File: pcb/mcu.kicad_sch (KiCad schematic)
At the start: 19 parts, among them J4 AVR-UPDI-6, U4 ATtiny1616-MNR

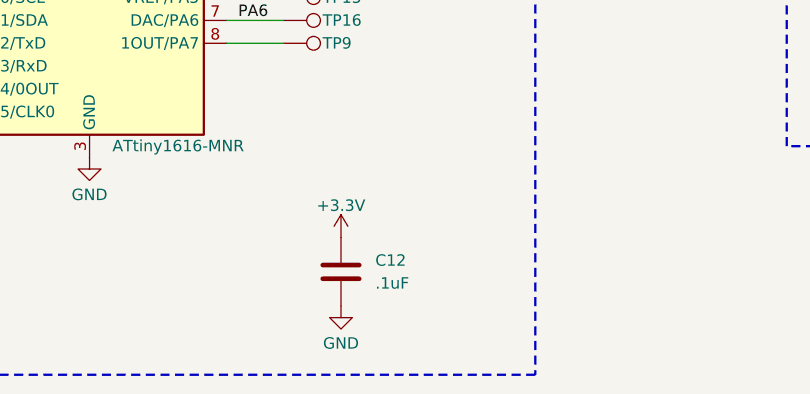
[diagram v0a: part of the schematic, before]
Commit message: Fixed LCSC part numbers and attributes
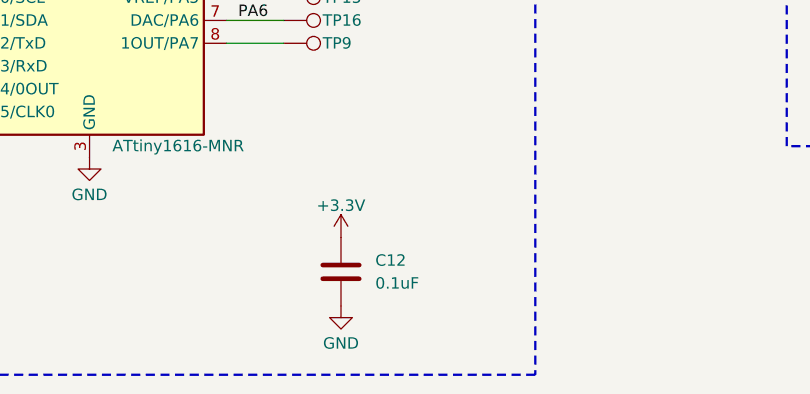
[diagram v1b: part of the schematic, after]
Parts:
- C12: value .1uF -> 0.1uF; LCSC C15849 -> C66501; MPN CL10A105KB8NNNC -> CL10B104KO8NNNC; Tolerance (none) -> 10%
- R13, R14: Tolerance (none) -> 5%
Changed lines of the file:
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@@
 			)
 		)
-		(property "Value" ".1uF"
+		(property "Value" "0.1uF"
 			(at 132.08 88.8999 0)
 			(effects
@@
 			)
 		)
-		(property "MPN" "CL10A105KB8NNNC"
+		(property "MPN" "CL10B104KO8NNNC"
 			(at 128.27 87.63 0)
 			(effects
@@
 			)
 		)
-		(property "LCSC" "C15849"
+		(property "LCSC" "C66501"
 			(at 128.27 87.63 0)
 			(effects
@@
 		)
 		(property "Mouser" "187-CL10A105KB8NNNC"
+			(at 128.27 87.63 0)
+			(effects
+				(font
+					(size 1.27 1.27)
+				)
+				(hide yes)
+			)
+		)
+		(property "Tolerance" "10%"
 			(at 128.27 87.63 0)
 			(effects
@@
 			)
 		)
+		(property "Tolerance" "5%"
+			(at 64.77 52.07 0)
+			(effects
+				(font
+					(size 1.27 1.27)
+				)
+				(hide yes)
+			)
+		)
 		(pin "2"
 		)
@@
 			(at 49.53 52.07 0)
 			(effects
+				(font
+					(size 1.27 1.27)
+				)
+				(hide yes)
+			)
+		)
+		(property "Tolerance" "5%"
+			(at 49.53 52.07 0)
+			(effects

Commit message: Adjusted BOM settings
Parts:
- C12: Digikey 1276-1860-2-ND -> 1276-1005-2-ND; Mouser 187-CL10A105KB8NNNC -> 187-CL10B104KO8NNNC; Vr (none) -> 16V
- TP10, TP11, TP12, TP13, TP14, TP15, TP16, TP18, TP7, TP8, TP9: now left out of the parts list
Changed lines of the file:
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@@
 		(unit 1)
 		(exclude_from_sim no)
-		(in_bom yes)
+		(in_bom no)
 		(on_board yes)
 		(dnp no)
@@
 		(unit 1)
 		(exclude_from_sim no)
-		(in_bom yes)
+		(in_bom no)
 		(on_board yes)
 		(dnp no)
@@
 		(unit 1)
 		(exclude_from_sim no)
-		(in_bom yes)
+		(in_bom no)
 		(on_board yes)
 		(dnp no)
@@
 		(unit 1)
 		(exclude_from_sim no)
-		(in_bom yes)
+		(in_bom no)
 		(on_board yes)
 		(dnp no)
@@
 			)
 		)
-		(property "Digikey" "1276-1860-2-ND"
+		(property "Digikey" "1276-1005-2-ND"
 			(at 128.27 87.63 0)
 			(effects
@@
 			)
 		)
-		(property "Mouser" "187-CL10A105KB8NNNC"
+		(property "Mouser" "187-CL10B104KO8NNNC"
 			(at 128.27 87.63 0)
 			(effects
@@
 		)
 		(property "Tolerance" "10%"
+			(at 128.27 87.63 0)
+			(effects
+				(font
+					(size 1.27 1.27)
+				)
+				(hide yes)
+			)
+		)
+		(property "Vr" "16V"
 			(at 128.27 87.63 0)
 			(effects
@@
 		(unit 1)
 		(exclude_from_sim no)
-		(in_bom yes)
+		(in_bom no)
 		(on_board yes)
 		(dnp no)
@@
 		(property "Description" "Test Point D1.0mm"
 			(at 195.58 47.244 0)
+			(effects
+				(font
+					(size 1.27 1.27)
+				)
+				(hide yes)
+			)
+		)
+		(property "LCSC" ""
+			(at 195.58 38.1 0)
+			(effects
+				(font
+					(size 1.27 1.27)
+				)
+				(hide yes)
+			)
+		)
+		(property "Digikey" ""
+			(at 195.58 38.1 0)
+			(effects
+				(font
+					(size 1.27 1.27)
+				)
+				(hide yes)
+			)
+		)
+		(property "Mouser" ""
+			(at 195.58 38.1 0)
 			(effects
 				(font
@@
 		(unit 1)
 		(exclude_from_sim no)
-		(in_bom yes)
+		(in_bom no)
 		(on_board yes)
 		(dnp no)
@@
 		(unit 1)
 		(exclude_from_sim no)
-		(in_bom yes)
+		(in_bom no)
 		(on_board yes)
 		(dnp no)
@@
 		(unit 1)
 		(exclude_from_sim no)
-		(in_bom yes)
+		(in_bom no)
 		(on_board yes)
 		(dnp no)
@@
 		(unit 1)
 		(exclude_from_sim no)
-		(in_bom yes)
+		(in_bom no)
 		(on_board yes)
 		(dnp no)
@@
 		(unit 1)
 		(exclude_from_sim no)
-		(in_bom yes)
+		(in_bom no)
 		(on_board yes)
 		(dnp no)
@@
 		(unit 1)
 		(exclude_from_sim no)
-		(in_bom yes)
-		(on_board yes)
-		(dnp no)
+		(in_bom no)
+		(on_board yes)
+		(dnp no)

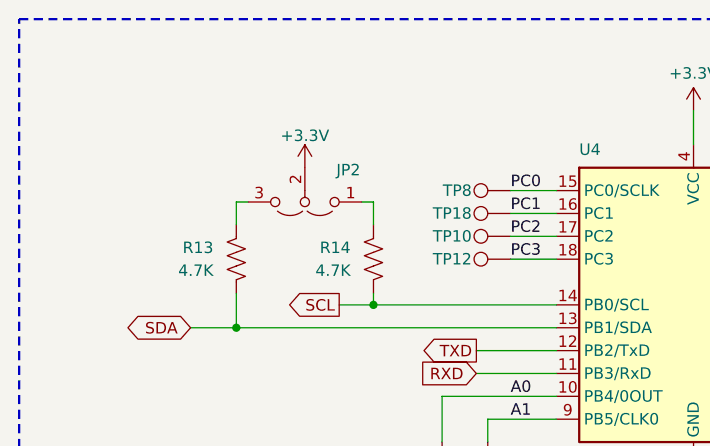
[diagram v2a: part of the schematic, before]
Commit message: Tightened to 50mm wide
SO MUCH fiddling!
Changed I2C to single jumpers
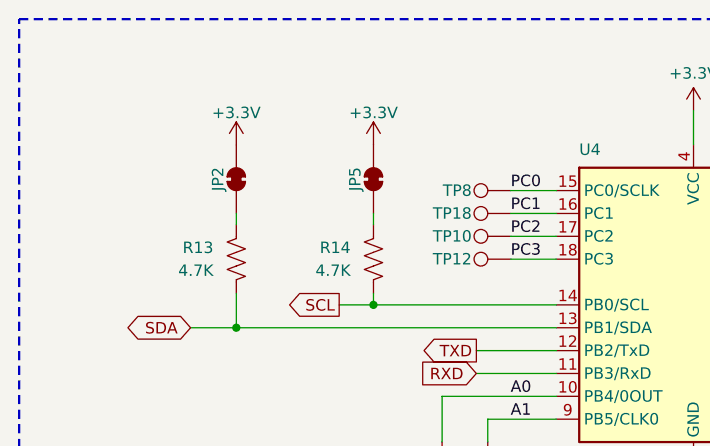
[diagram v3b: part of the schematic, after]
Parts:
- removed JP2: ~, CRGM Connector:SolderJumper-3_P1.3mm_Open_RoundedPad1.0x1.5mm, symbol Jumper:Jumper_3_Open
- added JP2, JP5: ~, CRGM Connector:SolderJumper-2_P1.3mm_Bridged_RoundedPad1.0x1.5mm, symbol Jumper:SolderJumper_2_Bridged
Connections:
- net +3.3V: now also JP2.2 (B), JP5.2 (B)
- net at R14.2: now also JP5.1 (A)
- net at R13.2: now also JP2.1 (A)
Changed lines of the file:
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@@
 	(wire
 		(pts
-			(xy 64.77 45.72) (xy 64.77 48.26)
+			(xy 64.77 46.99) (xy 64.77 48.26)
 		)
 		(stroke
@@
 	(wire
 		(pts
-			(xy 63.5 45.72) (xy 64.77 45.72)
-		)
-		(stroke
-			(width 0)
-			(type default)
-		)
-	)
-	(wire
-		(pts
 			(xy 217.17 46.99) (xy 220.98 46.99)
 		)
@@
 	(wire
 		(pts
-			(xy 50.8 45.72) (xy 49.53 45.72)
-		)
-		(stroke
-			(width 0)
-			(type default)
-		)
-	)
-	(wire
-		(pts
 			(xy 49.53 59.69) (xy 85.09 59.69)
 		)
@@
 	(wire
 		(pts
-			(xy 49.53 45.72) (xy 49.53 48.26)
+			(xy 49.53 46.99) (xy 49.53 48.26)
 		)
 		(stroke
@@
 				(path "/a8149920-3b7f-4d7d-8e96-7a0b38870225/573c51ea-89ab-4745-b6d8-c69e780cd603"
 					(reference "TP10")
+					(unit 1)
+				)
+			)
+		)
+	)
+	(symbol
+		(lib_id "Jumper:SolderJumper_2_Bridged")
+		(at 64.77 43.18 90)
+		(unit 1)
+		(exclude_from_sim no)
+		(in_bom no)
+		(on_board yes)
+		(dnp no)
+		(property "Reference" "JP5"
+			(at 62.738 43.18 0)
+			(effects
+				(font
+					(size 1.27 1.27)
+				)
+			)
+		)
+		(property "Value" "~"
+			(at 67.31 43.18 0)
+			(effects
+				(font
+					(size 1.27 1.27)
+				)
+				(hide yes)
+			)
+		)
+		(property "Footprint" "CRGM Connector:SolderJumper-2_P1.3mm_Bridged_RoundedPad1.0x1.5mm"
+			(at 64.77 43.18 0)
+			(effects
+				(font
+					(size 1.27 1.27)
+				)
+				(hide yes)
+			)
+		)
+		(property "Datasheet" "~"
+			(at 64.77 43.18 0)
+			(effects
+				(font
+					(size 1.27 1.27)
+				)
+				(hide yes)
+			)
+		)
+		(property "Description" "Solder Jumper, 2-pole, closed/bridged"
+			(at 64.77 43.18 0)
+			(effects
+				(font
+					(size 1.27 1.27)
+				)
+				(hide yes)
+			)
+		)
+		(property "LCSC" ""
+			(at 64.77 43.18 0)
+			(effects
+				(font
+					(size 1.27 1.27)
+				)
+				(hide yes)
+			)
+		)
+		(property "Digikey" ""
+			(at 64.77 43.18 0)
+			(effects
+				(font
+					(size 1.27 1.27)
+				)
+				(hide yes)
+			)
+		)
+		(property "Mouser" ""
+			(at 64.77 43.18 0)
+			(effects
+				(font
+					(size 1.27 1.27)
+				)
+				(hide yes)
+			)
+		)
+		(pin "2"
+		)
+		(pin "1"
+		)
+		(instances
+			(project "current-module"
+				(path "/a8149920-3b7f-4d7d-8e96-7a0b38870225/573c51ea-89ab-4745-b6d8-c69e780cd603"
+					(reference "JP5")
 					(unit 1)
 				)
@@
 	)
 	(symbol
-		(lib_id "Jumper:Jumper_3_Open")
-		(at 57.15 45.72 180)
-		(unit 1)
-		(exclude_from_sim no)
-		(in_bom no)
-		(on_board yes)
-		(dnp no)
-		(property "Reference" "JP2"
-			(at 61.976 42.164 0)
-			(effects
-				(font
-					(size 1.27 1.27)
-				)
-			)
-		)
-		(property "Value" "~"
-			(at 48.006 42.418 0)
-			(effects
-				(font
-					(size 1.27 1.27)
-				)
-			)
-		)
-		(property "Footprint" "CRGM Connector:SolderJumper-3_P1.3mm_Open_RoundedPad1.0x1.5mm"
-			(at 57.15 45.72 0)
-			(effects
-				(font
-					(size 1.27 1.27)
-				)
-				(hide yes)
-			)
-		)
-		(property "Datasheet" "~"
-			(at 57.15 45.72 0)
-			(effects
-				(font
-					(size 1.27 1.27)
-				)
-				(hide yes)
-			)
-		)
-		(property "Description" "Jumper, 3-pole, both open"
-			(at 57.15 45.72 0)
-			(effects
-				(font
-					(size 1.27 1.27)
-				)
-				(hide yes)
-			)
-		)
-		(property "MPN" ""
-			(at 57.15 45.72 0)
-			(effects
-				(font
-					(size 1.27 1.27)
-				)
-				(hide yes)
-			)
-		)
-		(property "LCSC" ""
-			(at 57.15 45.72 0)
-			(effects
-				(font
-					(size 1.27 1.27)
-				)
-				(hide yes)
-			)
-		)
-		(property "Digikey" ""
-			(at 57.15 45.72 0)
-			(effects
-				(font
-					(size 1.27 1.27)
-				)
-				(hide yes)
-			)
-		)
-		(property "Mouser" ""
-			(at 57.15 45.72 0)
-			(effects
-				(font
-					(size 1.27 1.27)
-				)
-				(hide yes)
-			)
-		)
-		(pin "3"
-		)
-		(pin "1"
-		)
-		(pin "2"
-		)
-		(instances
-			(project "relay-module"
-				(path "/445c1fff-2e1a-48b1-a91f-a137832edebf/3b602092-7627-4b1e-9a45-58db61fac69b"
-					(reference "JP1")
-					(unit 1)
-				)
-			)
-			(project ""
-				(path "/a8149920-3b7f-4d7d-8e96-7a0b38870225/573c51ea-89ab-4745-b6d8-c69e780cd603"
-					(reference "JP2")
-					(unit 1)
-				)
-			)
-		)
-	)
-	(symbol
 		(lib_id "power:+3.3V")
-		(at 57.15 41.91 0)
+		(at 49.53 39.37 0)
 		(mirror y)
 		(unit 1)
@@
 		(dnp no)
 		(property "Reference" "#PWR0107"
-			(at 57.15 45.72 0)
+			(at 49.53 43.18 0)
 			(effects
 				(font
@@
 		)
 		(property "Value" "+3.3V"
-			(at 57.15 38.354 0)
+			(at 49.53 35.814 0)
 			(effects
 				(font
@@
 		)
 		(property "Footprint" ""
-			(at 57.15 41.91 0)
+			(at 49.53 39.37 0)
 			(effects
 				(font
@@
 		)
 		(property "Datasheet" ""
-			(at 57.15 41.91 0)
+			(at 49.53 39.37 0)
 			(effects
 				(font
@@
 		)
 		(property "Description" "Power symbol creates a global label with name \"+3.3V\""
-			(at 57.15 41.91 0)
+			(at 49.53 39.37 0)
 			(effects
 				(font
@@
 				(path "/a8149920-3b7f-4d7d-8e96-7a0b38870225/573c51ea-89ab-4745-b6d8-c69e780cd603"
 					(reference "#PWR0107")
+					(unit 1)
+				)
+			)
+		)
+	)
+	(symbol
+		(lib_id "power:+3.3V")
+		(at 64.77 39.37 0)
+		(mirror y)
+		(unit 1)
+		(exclude_from_sim no)
+		(in_bom yes)
+		(on_board yes)
+		(dnp no)
+		(property "Reference" "#PWR03"
+			(at 64.77 43.18 0)
+			(effects
+				(font
+					(size 1.27 1.27)
+				)
+				(hide yes)
+			)
+		)
+		(property "Value" "+3.3V"
+			(at 64.77 35.814 0)
+			(effects
+				(font
+					(size 1.27 1.27)
+				)
+			)
+		)
+		(property "Footprint" ""
+			(at 64.77 39.37 0)
+			(effects
+				(font
+					(size 1.27 1.27)
+				)
+				(hide yes)
+			)
+		)
+		(property "Datasheet" ""
+			(at 64.77 39.37 0)
+			(effects
+				(font
+					(size 1.27 1.27)
+				)
+				(hide yes)
+			)
+		)
+		(property "Description" "Power symbol creates a global label with name \"+3.3V\""
+			(at 64.77 39.37 0)
+			(effects
+				(font
+					(size 1.27 1.27)
+				)
+				(hide yes)
+			)
+		)
+		(pin "1"
+		)
+		(instances
+			(project "current-module"
+				(path "/a8149920-3b7f-4d7d-8e96-7a0b38870225/573c51ea-89ab-4745-b6d8-c69e780cd603"
+					(reference "#PWR03")
 					(unit 1)
 				)
@@
 					(unit 1)
 				)
+			)
+		)
+	)
+	(symbol
+		(lib_id "Jumper:SolderJumper_2_Bridged")
+		(at 49.53 43.18 90)
+		(unit 1)
+		(exclude_from_sim no)
+		(in_bom no)
+		(on_board yes)
+		(dnp no)
+		(property "Reference" "JP2"
+			(at 47.498 43.18 0)
+			(effects
+				(font
+					(size 1.27 1.27)
+				)
+			)
+		)
+		(property "Value" "~"
+			(at 52.07 43.18 0)
+			(effects
+				(font
+					(size 1.27 1.27)
+				)
+				(hide yes)
+			)
+		)
+		(property "Footprint" "CRGM Connector:SolderJumper-2_P1.3mm_Bridged_RoundedPad1.0x1.5mm"
+			(at 49.53 43.18 0)
+			(effects
+				(font
+					(size 1.27 1.27)
+				)
+				(hide yes)
+			)
+		)
+		(property "Datasheet" "~"
+			(at 49.53 43.18 0)
+			(effects
+				(font
+					(size 1.27 1.27)
+				)
+				(hide yes)
+			)
+		)
+		(property "Description" "Solder Jumper, 2-pole, closed/bridged"
+			(at 49.53 43.18 0)
+			(effects
+				(font
+					(size 1.27 1.27)
+				)
+				(hide yes)
+			)
+		)
+		(property "LCSC" ""
+			(at 49.53 43.18 0)
+			(effects
+				(font
+					(size 1.27 1.27)
+				)
+				(hide yes)
+			)
+		)
+		(property "Digikey" ""
+			(at 49.53 43.18 0)
+			(effects
+				(font
+					(size 1.27 1.27)
+				)
+				(hide yes)
+			)
+		)
+		(property "Mouser" ""
+			(at 49.53 43.18 0)
+			(effects
+				(font
+					(size 1.27 1.27)
+				)
+				(hide yes)
+			)
+		)
+		(pin "2"
+		)
+		(pin "1"
+		)
+		(instances
+			(project "current-module"
+				(path "/a8149920-3b7f-4d7d-8e96-7a0b38870225/573c51ea-89ab-4745-b6d8-c69e780cd603"
+					(reference "JP2")
+					(unit 1)
+				)
